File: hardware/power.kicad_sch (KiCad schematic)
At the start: 0 parts

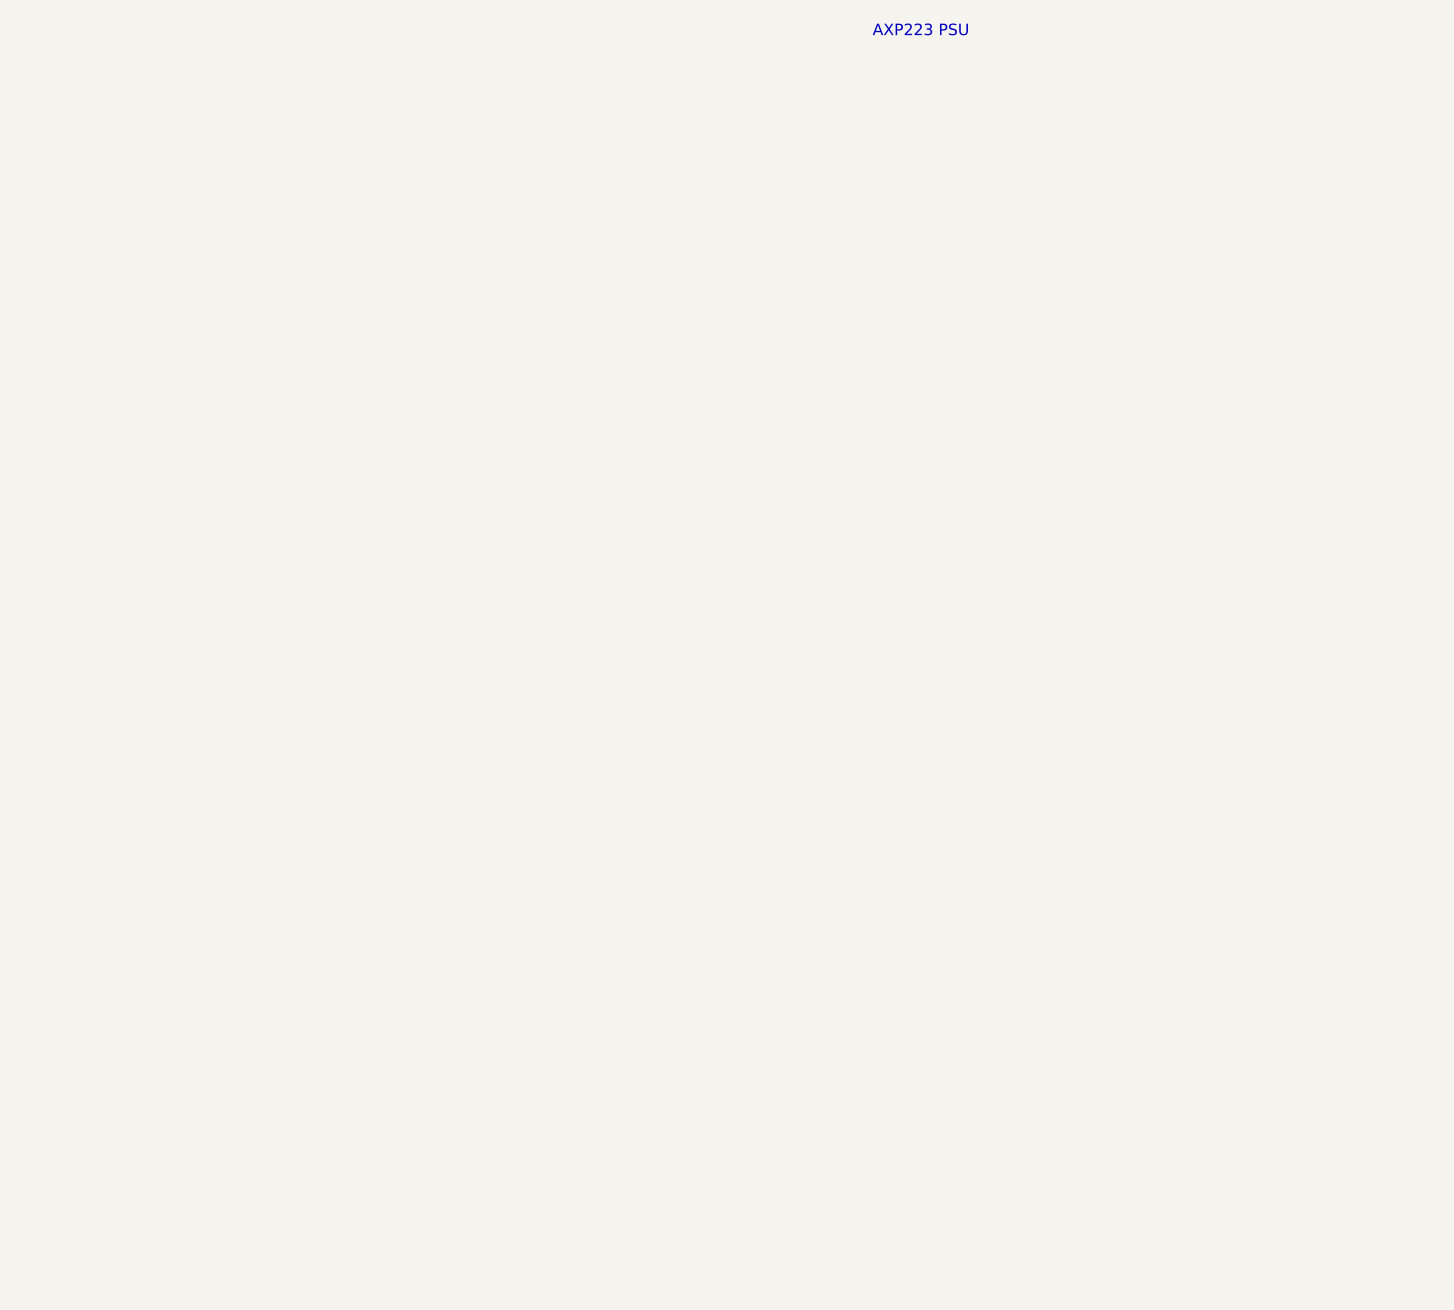
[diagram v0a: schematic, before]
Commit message: Start of psu
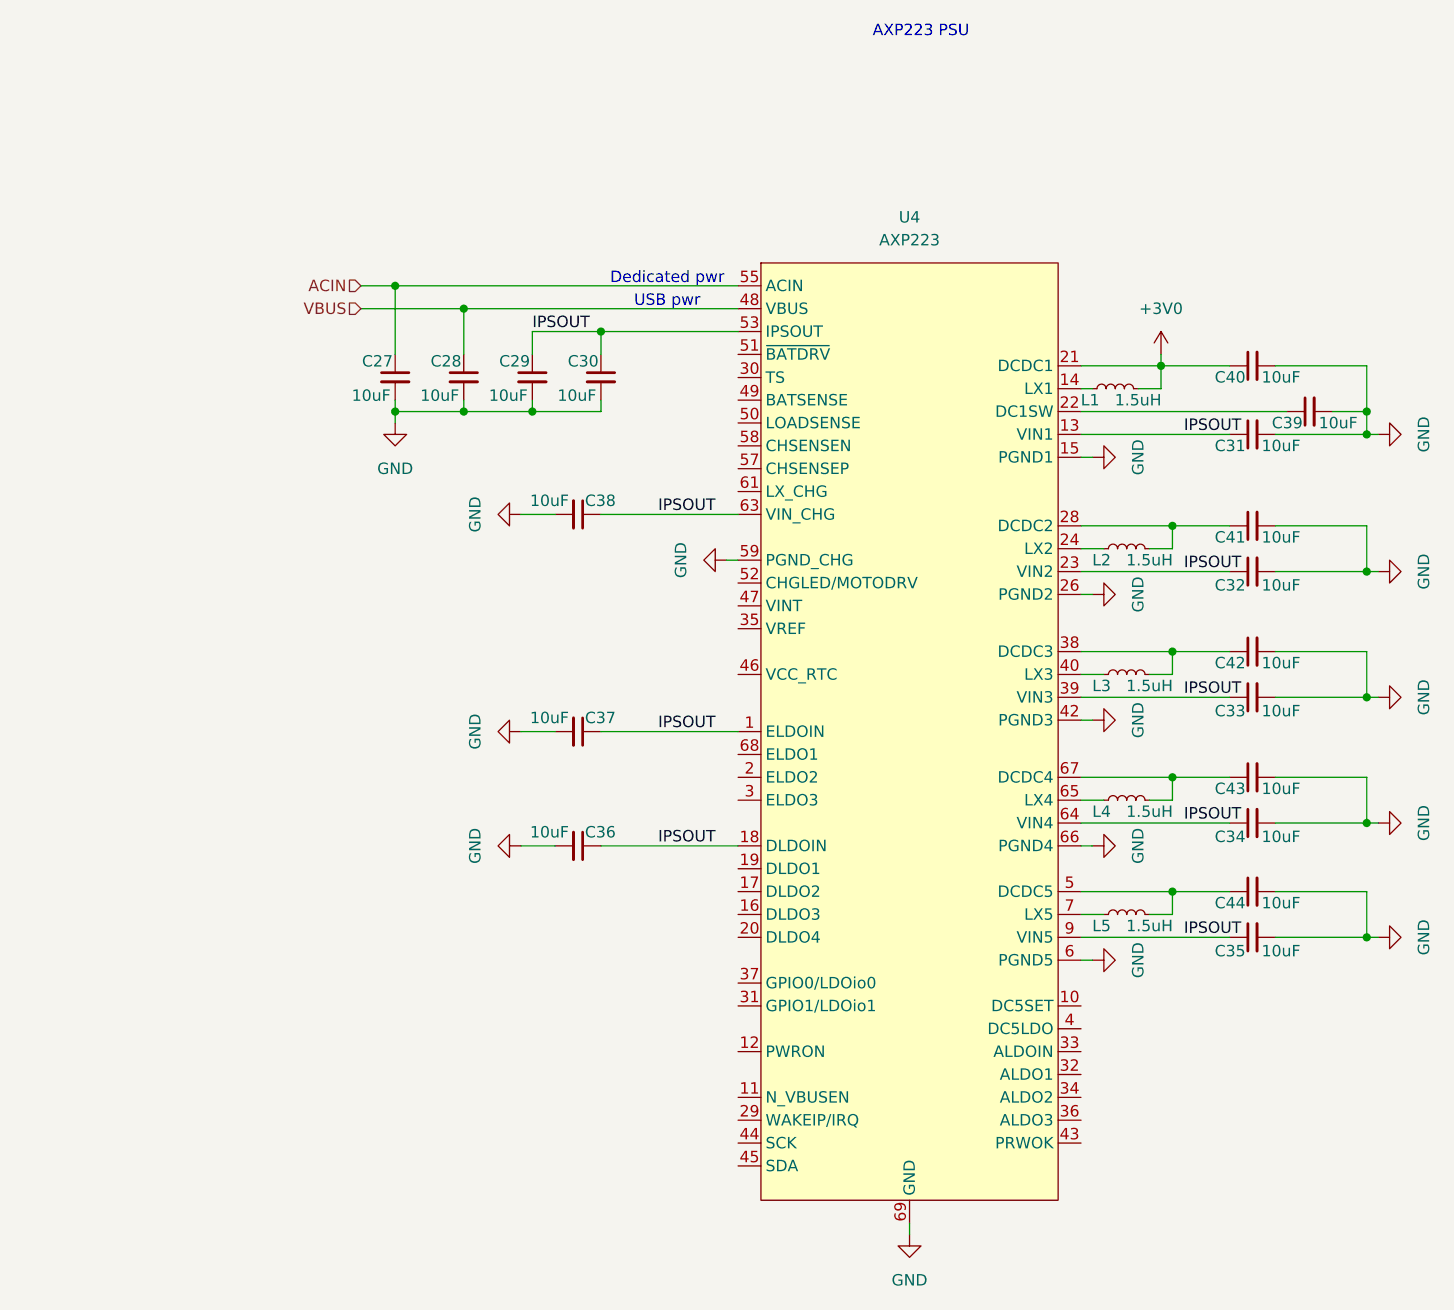
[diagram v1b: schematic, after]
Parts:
- added C27, C28, C29, C30, C31, C32, C33, C34, C35, C36, C37, C38, C39, C40, C41, C42, C43, C44: 10uF, symbol Device:C_Small
- added L1, L2, L3, L4, L5: 1.5uH, symbol Device:L_Small
- added U4: AXP223, slate-lib:QFN-68-1EP_8x8mm_P0.4mm_EP5.49x5.49mm, symbol slate-lib:AXP223
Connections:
- new net: L3.1, U4.40 (LX3), U4.41 (LX3)
- new net: C42.1, L3.2, U4.38 (DCDC3)
- new net: L4.1, U4.65 (LX4)
- new net: C43.1, L4.2, U4.67 (DCDC4)
- new net: L2.1, U4.24 (LX2), U4.25 (LX2)
- new net: C41.1, L2.2, U4.28 (DCDC2)
- new net: L1.1, U4.14 (LX1)
- new net: C39.1, U4.22 (DC1SW)
- new net: C44.1, L5.2, U4.5 (DCDC5)
- new net: U4.60 (LX_CHG), U4.61 (LX_CHG)
- new net: L5.1, U4.7 (LX5), U4.8 (LX5)
- new net +3V0: C40.1, L1.2, U4.21 (DCDC1)
- new net ACIN: C27.1, U4.55 (ACIN), U4.56 (ACIN)
- new net GND: C27.2, C28.2, C29.2, C30.2, C31.2, C32.2, C33.2, C34.2, C35.2, C36.2, C37.2, C38.2, C39.2, C40.2, C41.2, C42.2, C43.2, C44.2, U4.15 (PGND1), U4.26 (PGND2), U4.27 (PGND2), U4.42 (PGND3), U4.59 (PGND_CHG), U4.6 (PGND5), U4.66 (PGND4), U4.69 (GND)
- new net IPSOUT: C29.1, C30.1, C31.1, C32.1, C33.1, C34.1, C35.1, C36.1, C37.1, C38.1, U4.1 (ELDOIN), U4.13 (VIN1), U4.18 (DLDOIN), U4.23 (VIN2), U4.39 (VIN3), U4.53 (IPSOUT), U4.54 (IPSOUT), U4.62 (VIN_CHG), U4.63 (VIN_CHG), U4.64 (VIN4), U4.9 (VIN5)
- new net VBUS: C28.1, U4.48 (VBUS)
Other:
- note added: "Dedicated pwr"
- note added: "USB pwr"

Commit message: PMU 90% done
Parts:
- added C45, C46, C47, C48, C49, C50, C51, C52, C53, C55, C56, C57, C58, C60, C61, C62, C63, C64, C65, C66: 10uF, symbol Device:C_Small
- added C54: 1uF, symbol Device:C_Small
- added C59: 100nF, symbol Device:C_Small
- added D1: YELLOW, LED_SMD:LED_0603_1608Metric, symbol Device:LED_Small
- added L6: 1.5uH, symbol Device:L_Small
- added Q1: Si2301CDS, PCM_Package_TO_SOT_SMD_AKL:SOT-23, symbol PCM_Transistor_MOSFET_AKL:Si2301CDS
- added R11, R12: 2.2k, symbol Device:R
- added R13: 10k, symbol Device:R
- added R14, R17: 2k, symbol Device:R
- added R15, R16: 10m, symbol Device:R_Small
- added SW1: POWER_BTN, symbol Switch:SW_Push
- C38: value 10uF -> 1uF
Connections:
- net +3V0: now also R11.2, R12.2, R13.2
- net GND: now also U4.10 (DC5SET), U4.30 (TS), C45.2, C46.2, C47.2, C48.2, C49.2, C50.2, C51.2, C52.2, C53.2, C55.2, C56.2, C57.2, C58.2, C60.2, C61.2, C62.2, C63.2, C64.2, C65.2, C66.2, SW1.2; no longer C38.2, U4.69 (GND)
- net IPSOUT: now also U4.33 (ALDOIN), C56.1, C60.1, D1.2 (A), Q1.2 (S); no longer C38.1
- net +1V1-CPU: now reaches C42.1, L3.2, U4.38 (DCDC3)
- net DCDC4: now reaches C43.1, L4.2, U4.67 (DCDC4)
- net +1V1-SYS: now reaches C41.1, L2.2, U4.28 (DCDC2)
- net ~{PMU_VBUSEN}: now reaches U4.11 (N_VBUSEN)
- net PWRON: now reaches U4.12 (PWRON)
- net PWRON: now also C59.1, R17.1
- net DLDO3: now reaches U4.16 (DLDO3)
- net DLDO3: now also C47.1
- net DLDO2: now reaches U4.17 (DLDO2)
- net DLDO2: now also C46.1
- net DLDO1: now reaches U4.19 (DLDO1)
- net DLDO1: now also C45.1
- net ELDO2: now reaches U4.2 (ELDO2)
- net ELDO2: now also C50.1
- net DLDO4: now reaches U4.20 (DLDO4)
- net DLDO4: now also C48.1
- net PMU_IRQ: now reaches U4.29 (WAKEIP/IRQ)
- net PMU_IRQ: now also R13.1
- net ELDO3: now reaches U4.3 (ELDO3)
- net ELDO3: now also C51.1
- net at U4.31 (GPIO1/LDOio1): now also C66.1
- net ALDO1: now reaches U4.32 (ALDO1)
- net ALDO1: now also C61.1
- net ALDO2: now reaches U4.34 (ALDO2)
- net ALDO2: now also C62.1
- net at U4.35 (VREF): now also C53.1
- net ALDO3: now reaches U4.36 (ALDO3)
- net ALDO3: now also C63.1
- net at U4.37 (GPIO0/LDOio0): now also C65.1
- net +1V1-CPUS: now reaches U4.4 (DC5LDO)
- net +1V1-CPUS: now also C64.1
- net PMU_SCK: now reaches U4.44 (SCK)
- net PMU_SCK: now also R11.1
- net PMU_SDA: now reaches U4.45 (SDA)
- net PMU_SDA: now also R12.1
- net 3V0-RTC: now reaches U4.46 (VCC_RTC)
- net at U4.47 (VINT): now also C52.1
- net +BATT: now reaches U4.49 (BATSENSE)
- net +BATT: now also C54.1, R16.2
- net +1V5: now reaches C44.1, L5.2, U4.5 (DCDC5)
- net at U4.50 (LOADSENSE): now also C38.1, U4.58 (CHSENSEN), C54.2, C55.1, Q1.3 (D), R15.2, R16.1
- net at U4.51 (~{BATDRV}): now also Q1.1 (G)
- net at U4.52 (CHGLED/MOTODRV): now also R14.2
- net at U4.57 (CHSENSEP): now also C38.2, C57.1, C58.1, L6.1, R15.1
- net at U4.60 (LX_CHG), U4.61 (LX_CHG): now also L6.2
- net ELDO1: now reaches U4.68 (ELDO1)
- net ELDO1: now also C49.1
- new net: C59.2, R17.2, SW1.1
- new net: D1.1 (K), R14.1
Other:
- note added: "SPI pull-ups not needed?"
- note added: "TODO: I/O"
- note added: "TODO: RESET"
- moved on the sheet: C27, C28, C29, C30, C31, C32, C33, C34, C35, C36, C37, C38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
